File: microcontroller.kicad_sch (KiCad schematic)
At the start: 0 parts

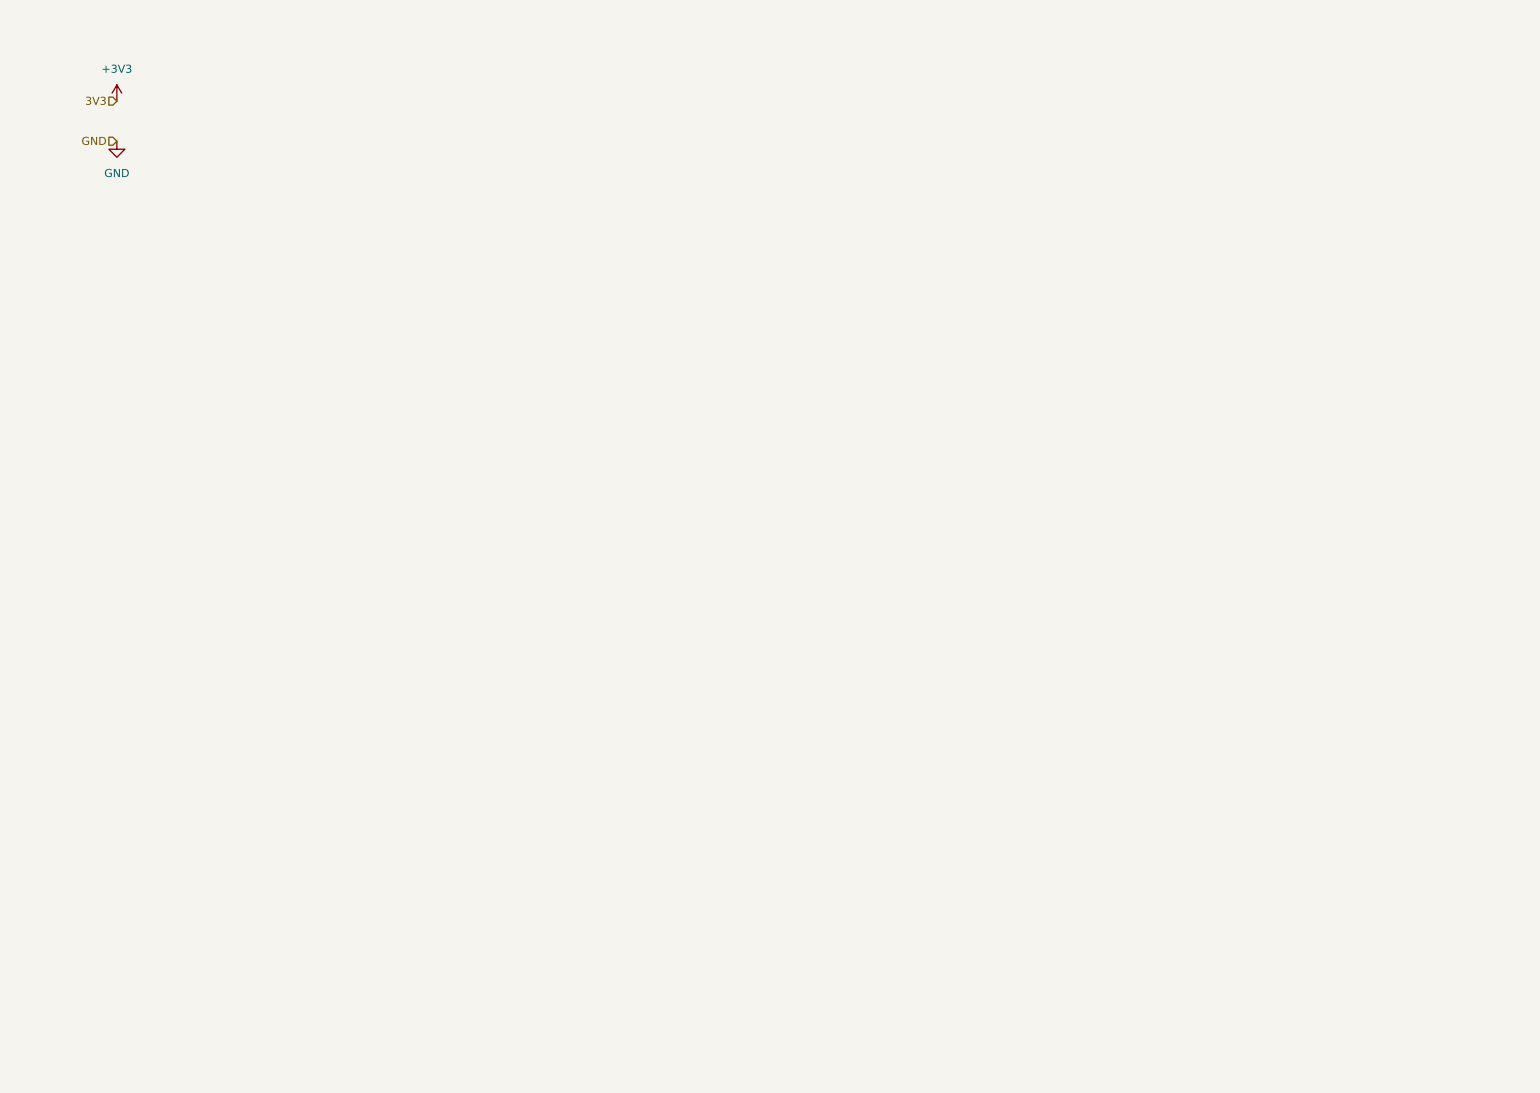
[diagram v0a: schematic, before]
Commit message: MCU Schem capture
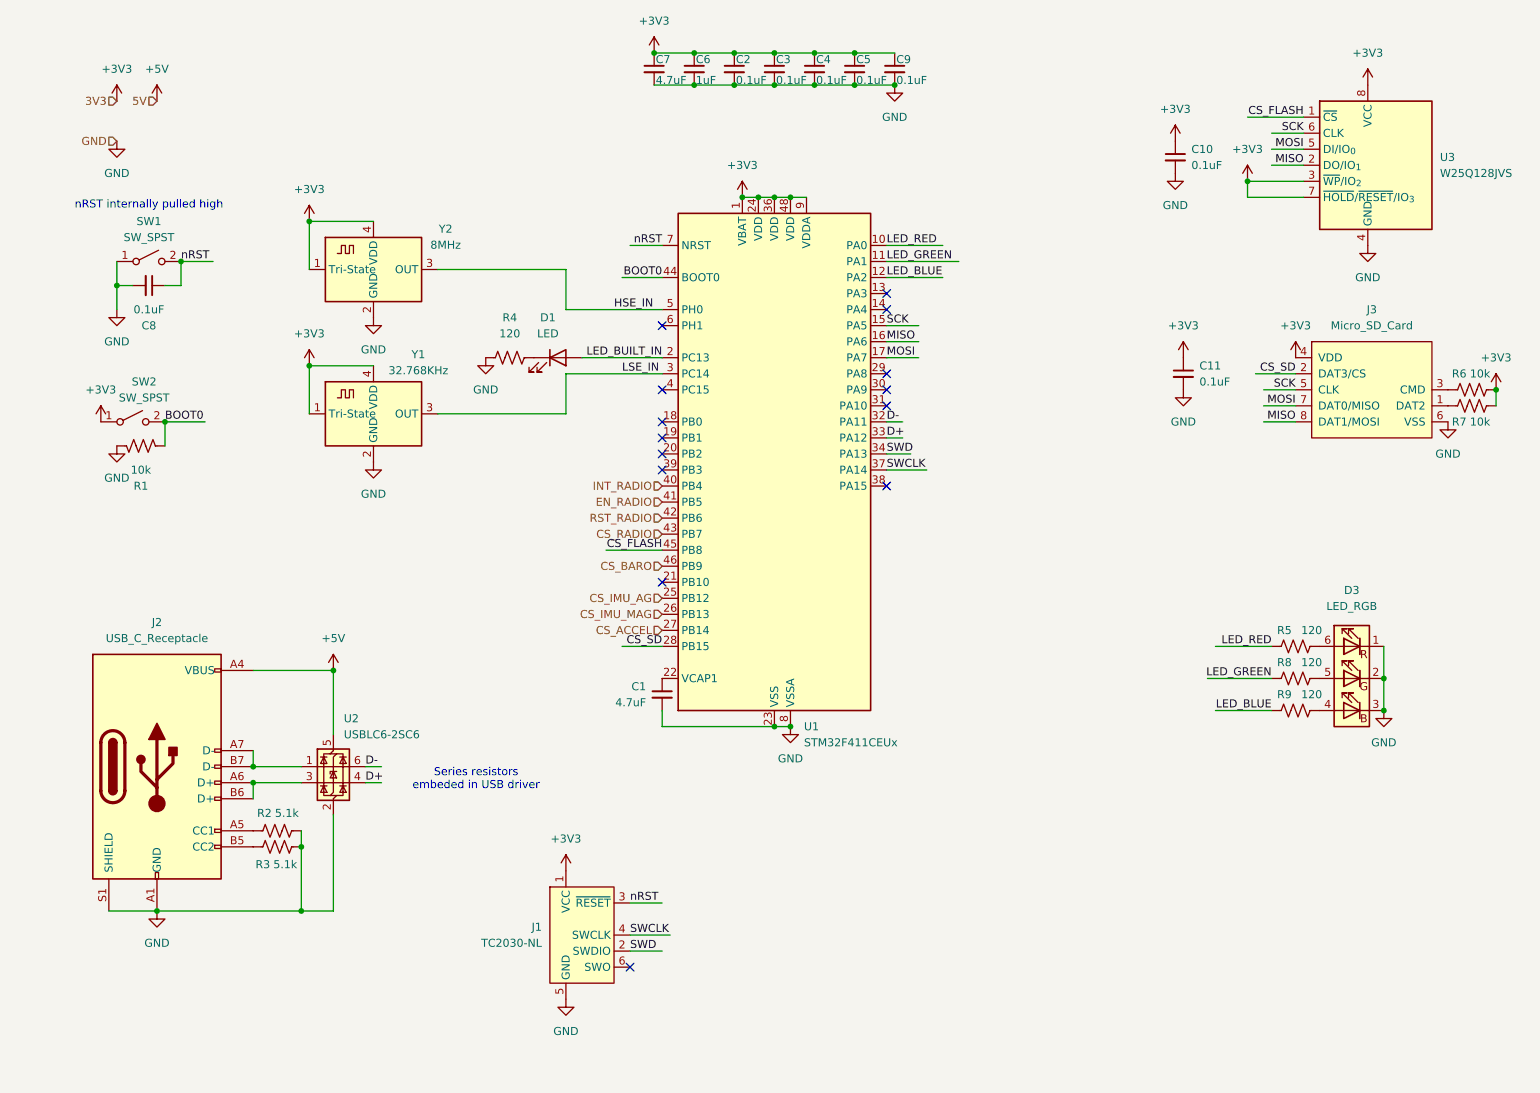
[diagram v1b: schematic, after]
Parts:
- added C1, C7: 4.7uF, symbol Device:C_Small
- added C10, C11, C2, C3, C4, C5, C8, C9: 0.1uF, symbol Device:C_Small
- added C6: 1uF, symbol Device:C_Small
- added D1: LED, symbol Device:LED
- added D3: LED_RGB, symbol Device:LED_RGB
- added J1: TC2030-NL, Connector:Tag-Connect_TC2030-IDC-NL_2x03_P1.27mm_Vertical, symbol Connector:Conn_ARM_SWD_TagConnect_TC2030-NL
- added J2: USB_C_Receptacle, symbol Connector:USB_C_Receptacle_USB2.0_14P
- added J3: Micro_SD_Card, symbol Avionics_Symbols:Micro_SD_Card
- added R1, R6, R7: 10k, symbol Device:R_US
- added R2, R3: 5.1k, symbol Device:R_US
- added R4, R5, R8, R9: 120, symbol Device:R_US
- added SW1, SW2: SW_SPST, symbol Switch:SW_SPST
- added U1: STM32F411CEUx, Package_DFN_QFN:QFN-48-1EP_7x7mm_P0.5mm_EP5.6x5.6mm, symbol MCU_ST_STM32F4:STM32F411CEUx
- added U2: USBLC6-2SC6, Package_TO_SOT_SMD:SOT-23-6, symbol Power_Protection:USBLC6-2SC6
- added U3: W25Q128JVS, Package_SO:SOIC-8_5.3x5.3mm_P1.27mm, symbol Memory_Flash:W25Q128JVS
- added Y1: 32.768KHz, Oscillator:Oscillator_SMD_Abracon_ASCO-4Pin_1.6x1.2mm, symbol Oscillator:ASCO
- added Y2: 8MHz, Oscillator:Oscillator_SMD_Abracon_ASCO-4Pin_1.6x1.2mm, symbol Oscillator:ASCO
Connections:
- net +3V3: now also C10.1, C11.1, C2.1, C3.1, C4.1, C5.1, C6.1, C7.1, C9.1, J1.1 (VCC), J3.4 (VDD), R6.2, R7.2, SW2.1 (A), U1.1 (VBAT), U1.24 (VDD), U1.36 (VDD), U1.48 (VDD), U1.9 (VDDA), U3.3 (~{WP}/IO_{2}), U3.7 (~{HOLD}/~{RESET}/IO_{3}), U3.8 (VCC), Y1.1 (Tri-State), Y1.4 (VDD), Y2.1 (Tri-State), Y2.4 (VDD)
- net GND: now also C1.2, C10.2, C11.2, C2.2, C3.2, C4.2, C5.2, C6.2, C7.2, C8.2, C9.2, D3.1 (RK), D3.2 (GK), D3.3 (BK), J1.5 (GND), J2.A1 (GND), J2.A12 (GND), J2.B1 (GND), J2.B12 (GND), J2.S1 (SHIELD), J3.6 (VSS), J3.G1 (GND), J3.G2 (GND), J3.G3 (GND), J3.G4 (GND), R1.1, R2.2, R3.2, R4.1, SW1.1 (A), U1.23 (VSS), U1.35 (VSS), U1.47 (VSS), U1.49 (VSS), U1.8 (VSSA), U2.2 (GND), U3.4 (GND), Y1.2 (GND), Y2.2 (GND)
- new net: C1.1, U1.22 (VCAP1)
- new net: D3.4 (BA), R9.2
- new net: J3.1 (DAT2), R7.1
- new net: J3.3 (CMD), R6.1
- new net: D3.6 (RA), R5.2
- new net: D1.1 (K), R4.2
- new net: J2.A5 (CC1), R2.1
- new net: J2.A7 (D-), J2.B7 (D-), U2.1 (I/O1)
- new net: J2.A6 (D+), J2.B6 (D+), U2.3 (I/O2)
- new net: J2.B5 (CC2), R3.1
- new net: D3.5 (GA), R8.2
- new net +5V: J2.A4 (VBUS), J2.A9 (VBUS), J2.B4 (VBUS), J2.B9 (VBUS), U2.5 (VBUS)
- new net BOOT0: R1.2, SW2.2 (B), U1.44 (BOOT0)
- new net CS_ACCEL: U1.27 (PB14)
- new net CS_BARO: U1.46 (PB9)
- new net CS_FLASH: U1.45 (PB8), U3.1 (~{CS})
- new net CS_IMU_AG: U1.25 (PB12)
- new net CS_IMU_MAG: U1.26 (PB13)
- new net CS_RADIO: U1.43 (PB7)
- new net CS_SD: J3.2 (DAT3/CS), U1.28 (PB15)
- new net D+: U1.33 (PA12), U2.4 (I/O2)
- new net D-: U1.32 (PA11), U2.6 (I/O1)
- new net EN_RADIO: U1.41 (PB5)
- new net HSE_IN: U1.5 (PH0), Y2.3 (OUT)
- new net INT_RADIO: U1.40 (PB4)
- new net LED_BLUE: R9.1, U1.12 (PA2)
- new net LED_BUILT_IN: D1.2 (A), U1.2 (PC13)
- new net LED_GREEN: R8.1, U1.11 (PA1)
- new net LED_RED: R5.1, U1.10 (PA0)
- new net LSE_IN: U1.3 (PC14), Y1.3 (OUT)
- new net MISO: J3.8 (DAT1/MOSI), U1.16 (PA6), U3.2 (DO/IO_{1})
- new net MOSI: J3.7 (DAT0/MISO), U1.17 (PA7), U3.5 (DI/IO_{0})
- new net RST_RADIO: U1.42 (PB6)
- new net SCK: J3.5 (CLK), U1.15 (PA5), U3.6 (CLK)
- new net SWCLK: J1.4 (SWCLK), U1.37 (PA14)
- new net SWD: J1.2 (SWDIO), U1.34 (PA13)
- new net nRST: C8.1, J1.3 (~{RESET}), SW1.2 (B), U1.7 (NRST)
- no-connect marks 0 -> 14
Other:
- note added: "Series resistors embeded in USB driver"
- note added: "nRST internally pulled high"

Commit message: Added bulk capacitnace
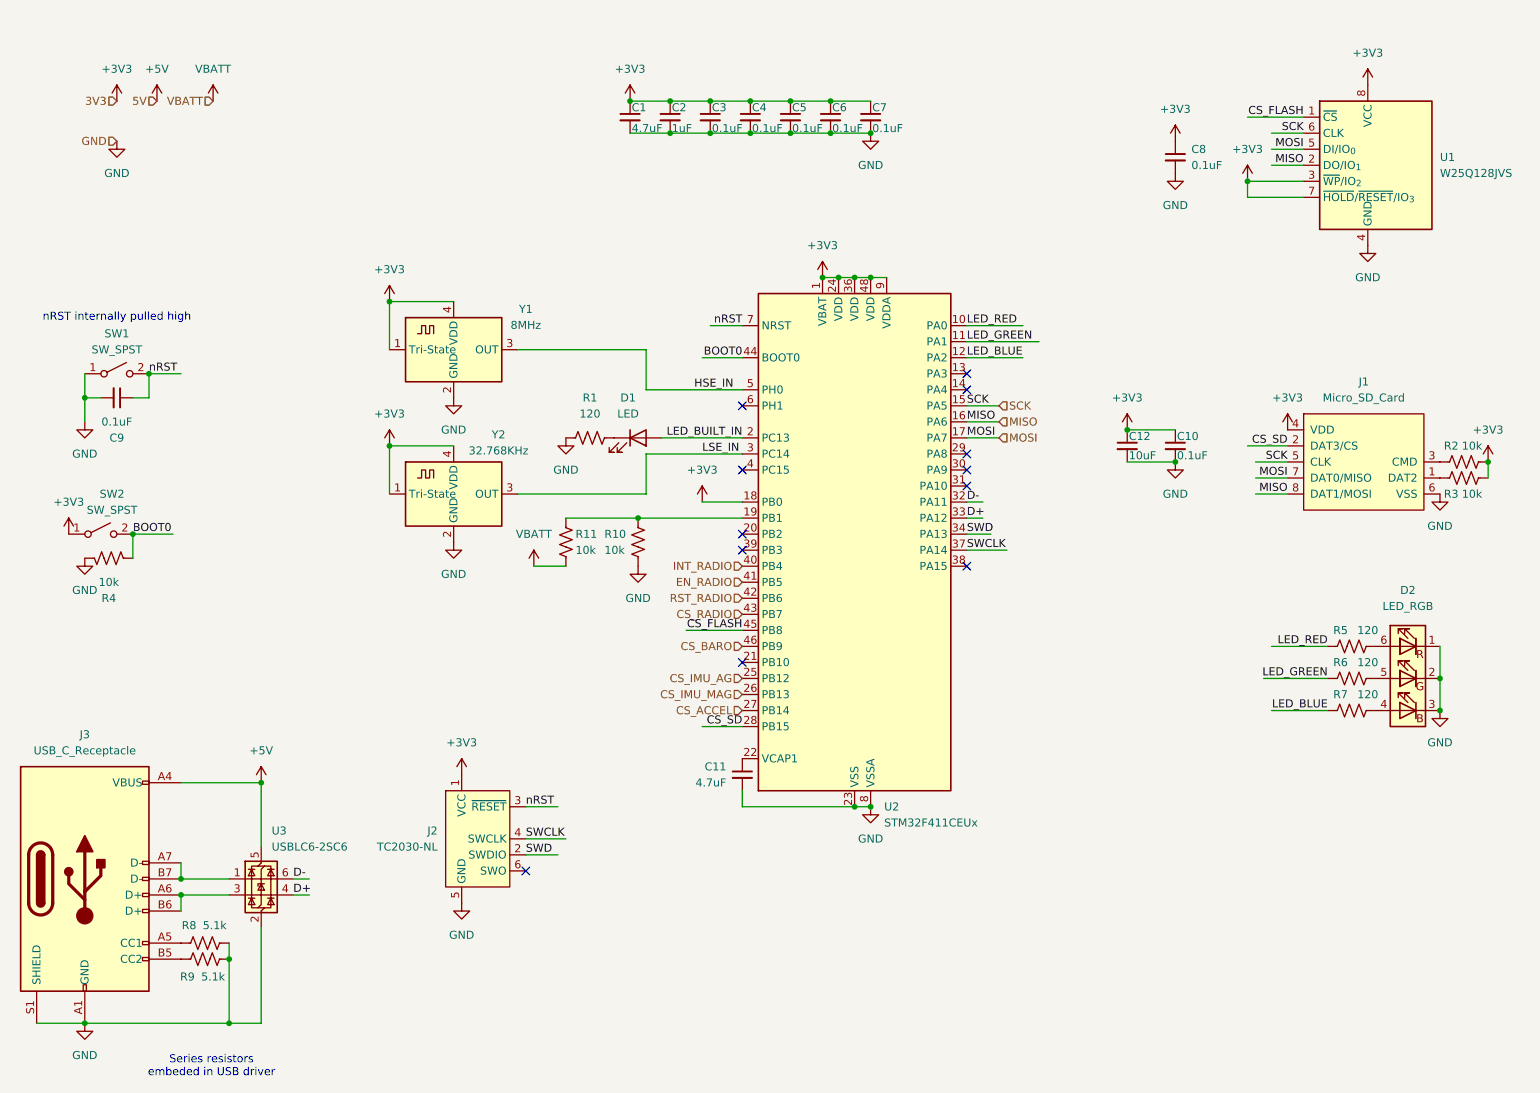
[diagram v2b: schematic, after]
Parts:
- added C12: 10uF, symbol Device:C_Small
- added R10, R11: 10k, symbol Device:R_US
- renumbered C7 to C1, C11 to C10, C1 to C11, C6 to C2, C2 to C3, C3 to C4, C4 to C5, C5 to C6, C9 to C7, C10 to C8, C8 to C9, D3 to D2, J3 to J1, J1 to J2, J2 to J3, R4 to R1, R6 to R2, R7 to R3, R1 to R4, R8 to R6, R9 to R7, R2 to R8, R3 to R9, U3 to U1, U1 to U2, U2 to U3, Y2 to Y1, Y1 to Y2
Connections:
- net +3V3: now also U2.18 (PB0), C12.1
- net GND: now also C12.2, R10.2
- net at U2.19 (PB1): now also R10.1, R11.1
- new net VBATT: R11.2
- no-connect marks 14 -> 12
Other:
- moved on the sheet: C1, C10, C11, C2, C3, C4, C5, C6, C7, C9, D1, D2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

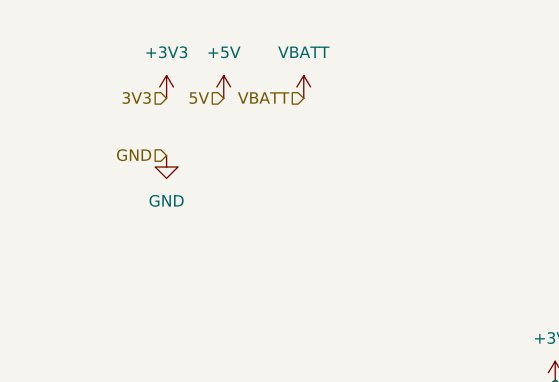
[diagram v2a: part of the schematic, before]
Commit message: Updated heiarchal power labels
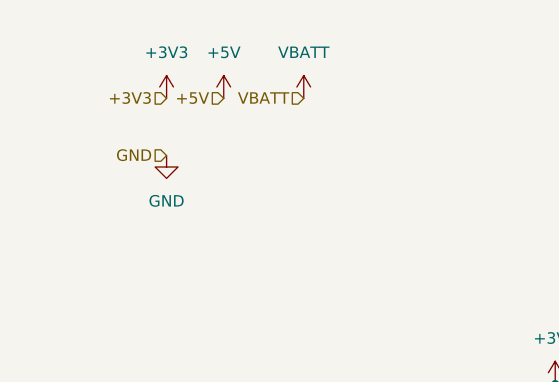
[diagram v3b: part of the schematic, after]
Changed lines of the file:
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@@
 		)
 	)
-	(hierarchical_label "5V"
+	(hierarchical_label "+5V"
 		(shape input)
 		(at 44.45 38.1 180)
@@
 		)
 	)
-	(hierarchical_label "3V3"
+	(hierarchical_label "+3V3"
 		(shape input)
 		(at 38.1 38.1 180)

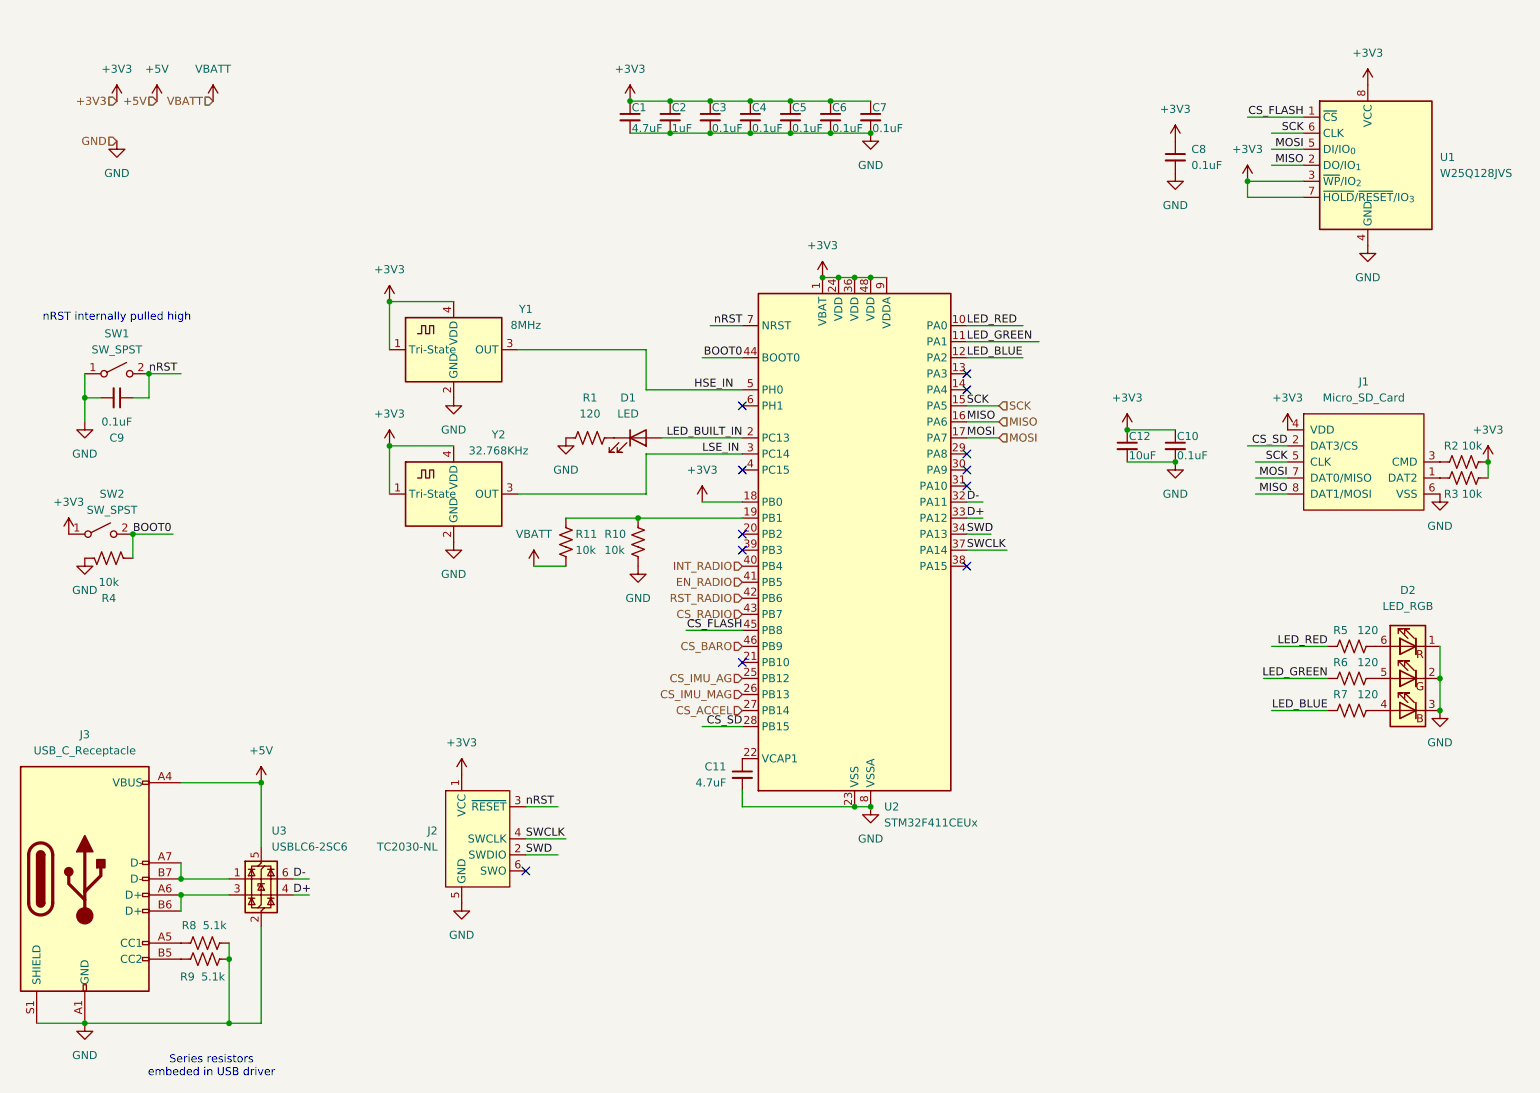
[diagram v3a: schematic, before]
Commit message: Moved labels, updated USB conn symbol
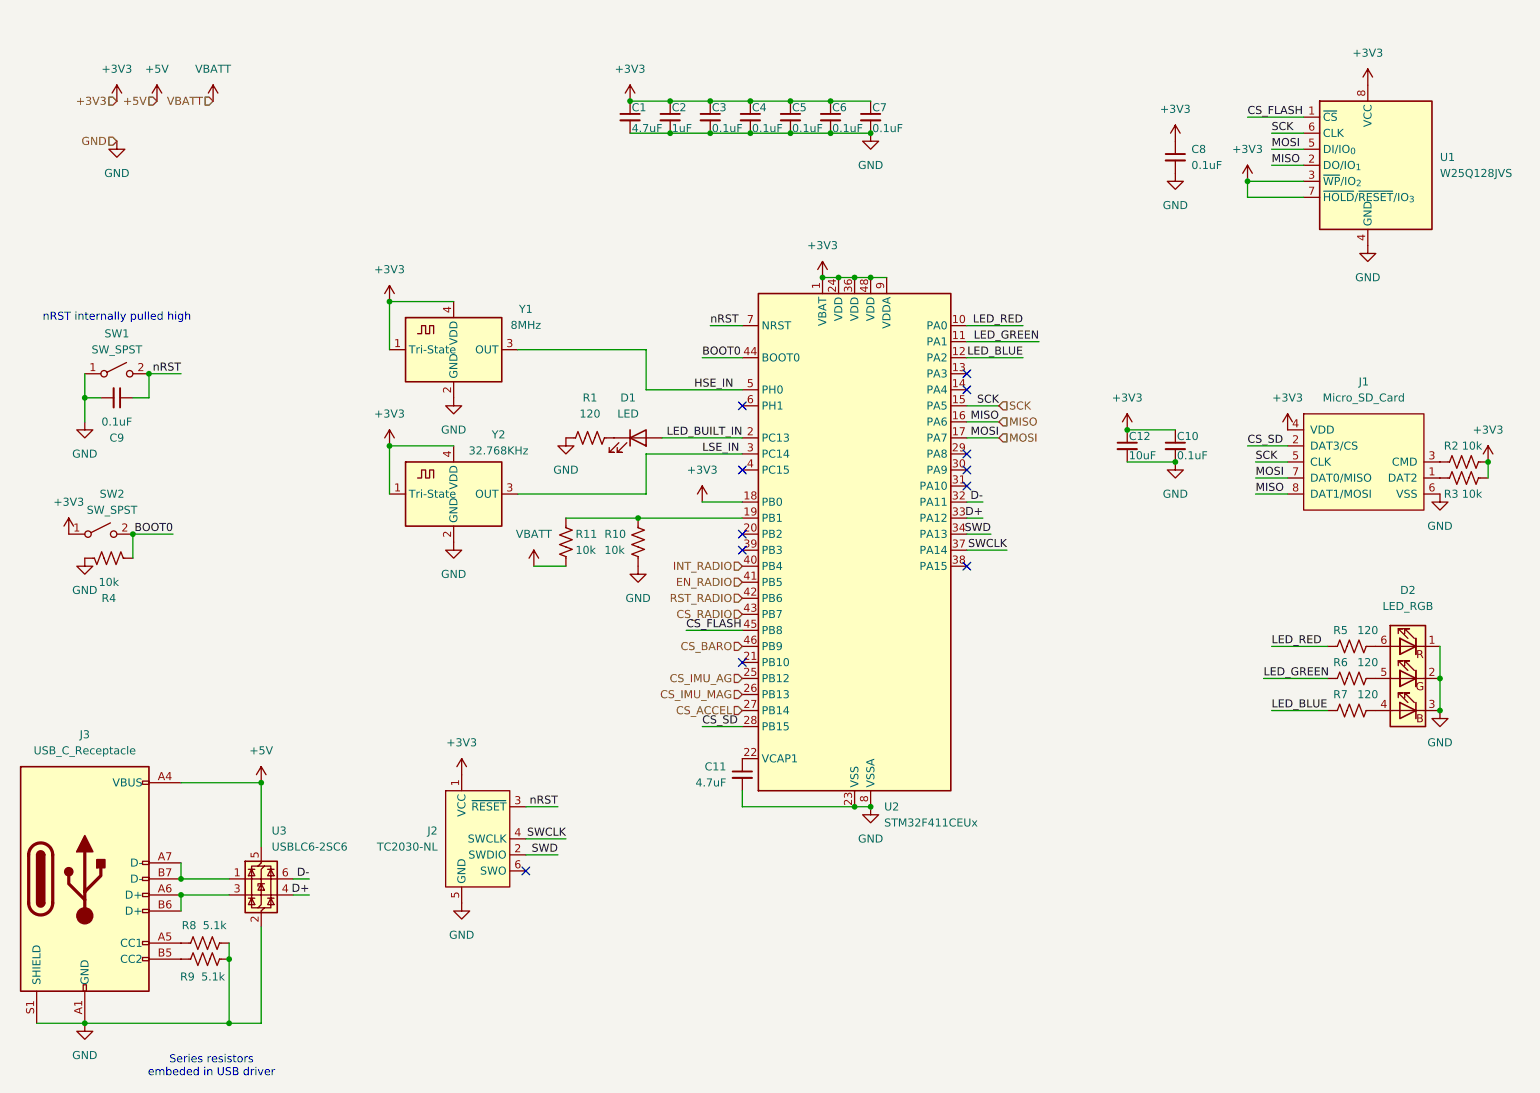
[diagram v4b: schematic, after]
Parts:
- J3: symbol Connector:USB_C_Receptacle_USB2.0_14P -> Avionics_Symbols:USB_C_Receptacle_USB2.0_14P_5V
